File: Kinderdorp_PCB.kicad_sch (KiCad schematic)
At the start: 39 parts, among them J1 Conn_01x08, Q1 2N7002_C306856, U2 AMS1117-3.3_C347222, U5 ESP32-C3-WROOM-02-N4(4MB)

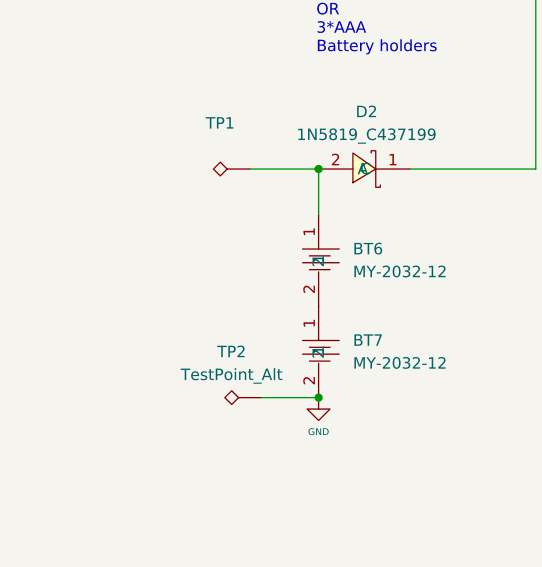
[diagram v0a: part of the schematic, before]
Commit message: added AAA box 3d model and reference images
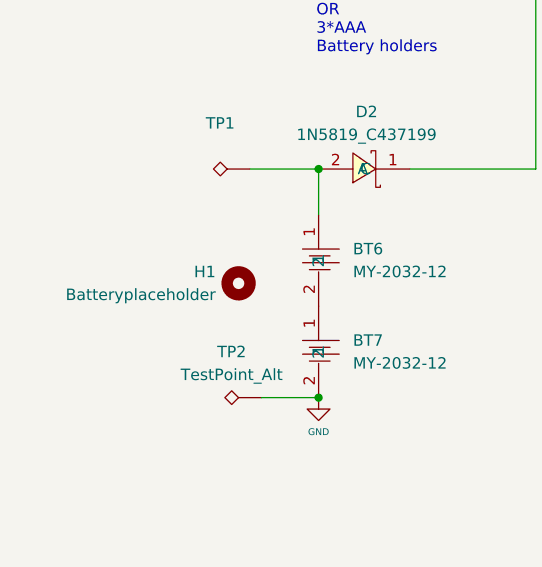
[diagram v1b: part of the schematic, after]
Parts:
- added H1: Batteryplaceholder, Capacitor_Tantalum_SMD:CP_EIA-1608-10_AVX-L, symbol Mechanical:MountingHole
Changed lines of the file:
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@@
+	)
+	(symbol
+		(lib_id "Mechanical:MountingHole")
+		(at 41.91 87.63 0)
+		(unit 1)
+		(exclude_from_sim no)
+		(in_bom no)
+		(on_board yes)
+		(dnp no)
+		(property "Reference" "H1"
+			(at 39.37 86.3599 0)
+			(effects
+				(font
+					(size 1.27 1.27)
+				)
+				(justify right)
+			)
+		)
+		(property "Value" "Batteryplaceholder"
+			(at 39.37 88.8999 0)
+			(effects
+				(font
+					(size 1.27 1.27)
+				)
+				(justify right)
+			)
+		)
+		(property "Footprint" "Capacitor_Tantalum_SMD:CP_EIA-1608-10_AVX-L"
+			(at 41.91 87.63 0)
+			(effects
+				(font
+					(size 1.27 1.27)
+				)
+				(hide yes)
+			)
+		)
+		(property "Datasheet" "~"
+			(at 41.91 87.63 0)
+			(effects
+				(font
+					(size 1.27 1.27)
+				)
+				(hide yes)
+			)
+		)
+		(property "Description" "Mounting Hole without connection"
+			(at 41.91 87.63 0)
+			(effects
+				(font
+					(size 1.27 1.27)
+				)
+				(hide yes)
+			)
+		)
+		(instances
+			(project ""
+				(path "/17f7643f-a16b-4802-8051-c0810a7f40c9"
+					(reference "H1")
+					(unit 1)
+				)
+			)
+		)
 	)
 	(symbol

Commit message: imported/created thumb design
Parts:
- H1: footprint Capacitor_Tantalum_SMD:CP_EIA-1608-10_AVX-L -> MountingHole:MountingHole_2.1mm
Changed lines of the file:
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@@
 			)
 		)
-		(property "Footprint" "Capacitor_Tantalum_SMD:CP_EIA-1608-10_AVX-L"
+		(property "Footprint" "MountingHole:MountingHole_2.1mm"
 			(at 41.91 87.63 0)
 			(effects

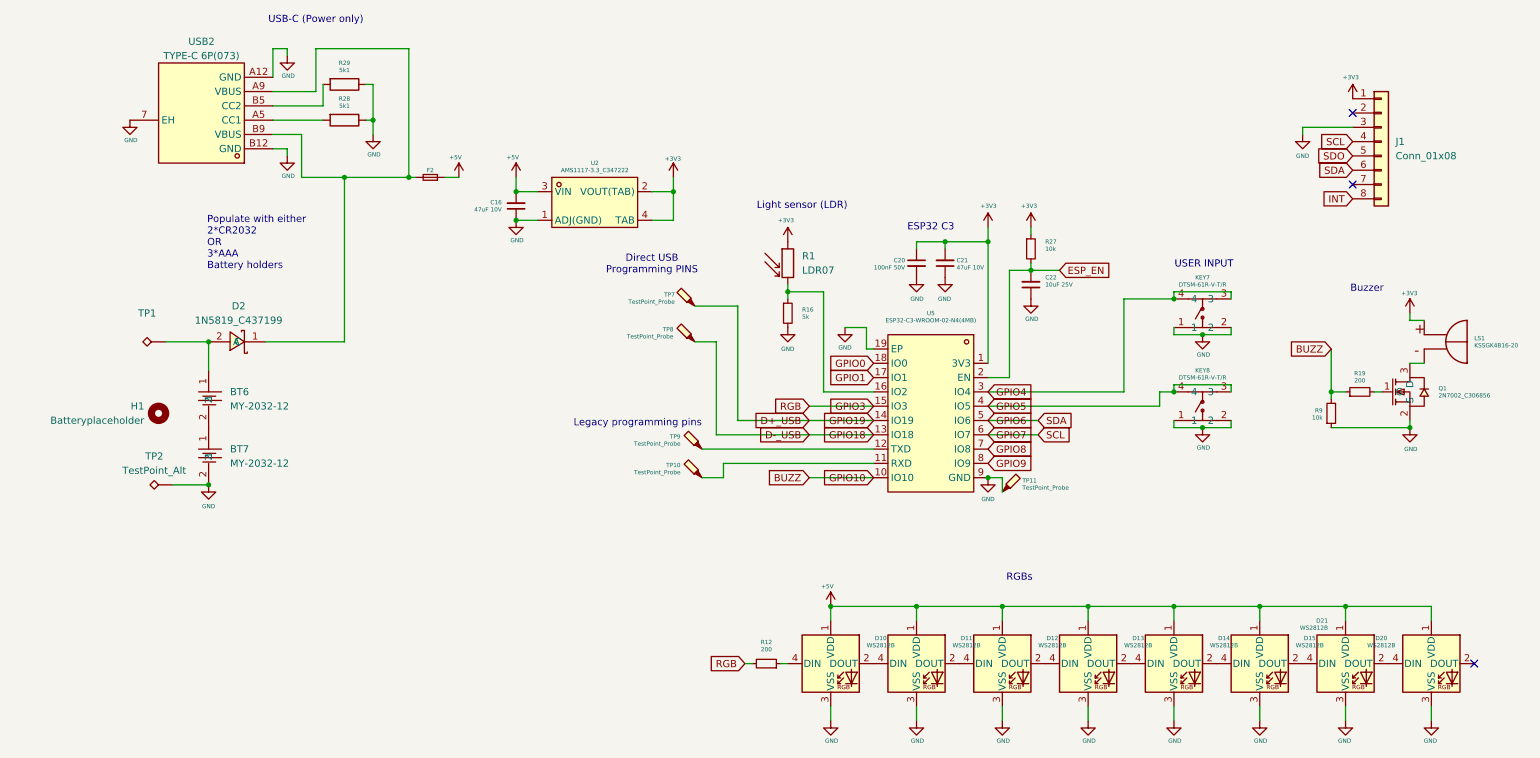
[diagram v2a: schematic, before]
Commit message: fixed naming designators
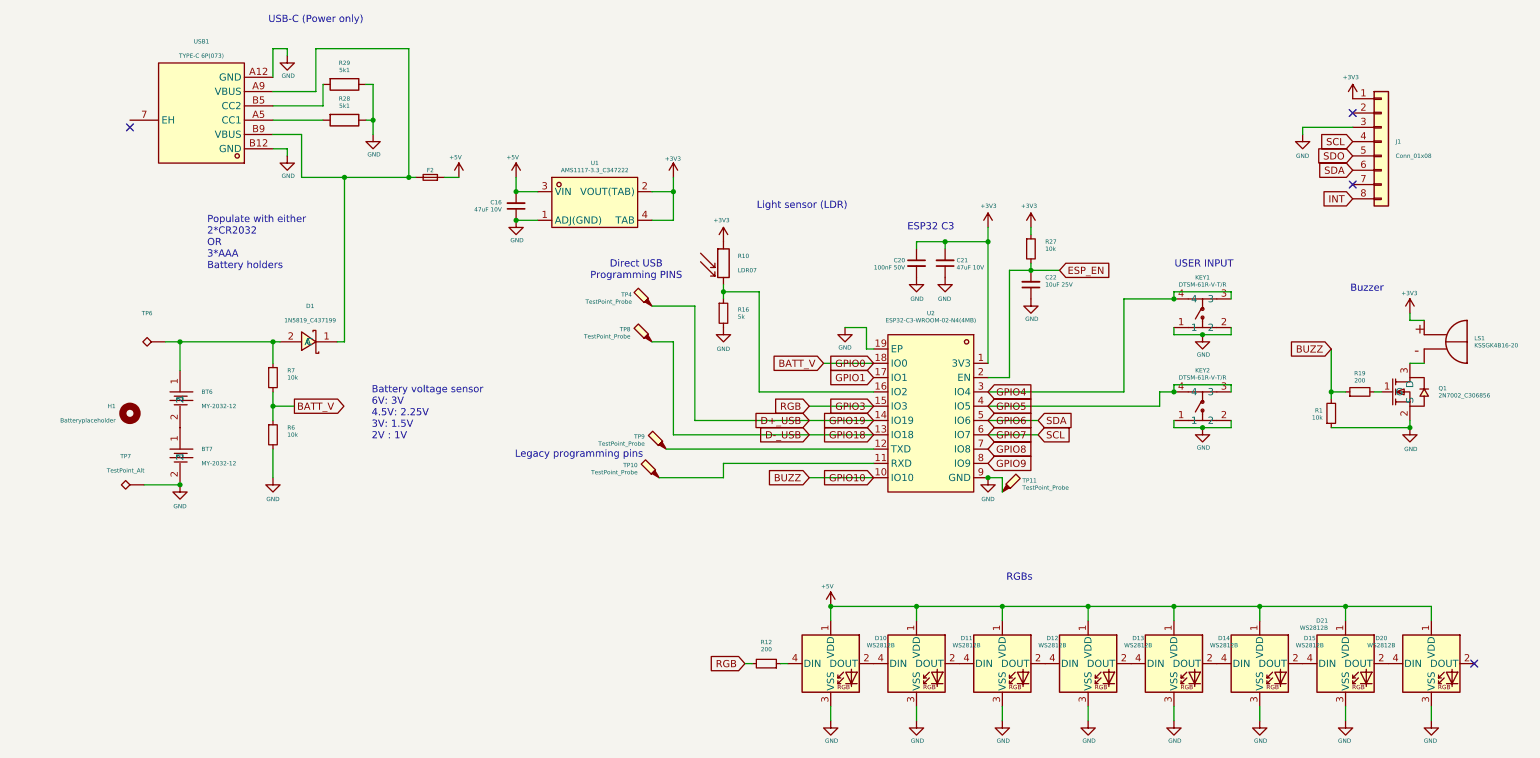
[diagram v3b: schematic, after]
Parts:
- added R6, R7: 10k, Resistor_SMD:R_1206_3216Metric_Pad1.30x1.75mm_HandSolder, symbol Device:R_Small
- renumbered D2 to D1, KEY7 to KEY1, KEY8 to KEY2, R9 to R1, R1 to R10, TP7 to TP4, TP1 to TP6, TP2 to TP7, U2 to U1, U5 to U2, USB2 to USB1
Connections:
- net GND: now also R6.2; no longer USB1.7 (EH)
- net at BT6.1, D1.2 (A), TP6.1: now also R7.1
- net GPIO0 renamed BATT_V
- net BATT_V: now also R6.1, R7.2
- no-connect marks 3 -> 4
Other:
- note added: "Battery voltage sensor 6V: 3V 4.5V: 2.25V 3V: 1.5V 2V : 1V"
- moved on the sheet: BT6, BT7, D1, H1, R10, R16, TP10, TP4, TP7, TP8, TP9

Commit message: fixed annotation again
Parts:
- renumbered BT6 to BT1, BT7 to BT2, KEY1 to BUTTON1, KEY2 to BUTTON2, C16 to C1, C20 to C2, C21 to C3, C22 to C4, F2 to F1, J1 to HDR1, R10 to LDR1, D10 to LED1, D11 to LED2, D12 to LED3, D13 to LED4, D14 to LED5, D15 to LED6, D21 to LED7, D20 to LED8, R7 to R1, R6 to R2, R29 to R3, R28 to R4, R16 to R5, R12 to R6, R27 to R7, R1 to R8, R19 to R9, TP7 to TP1, TP6 to TP2, TP4 to TP3, TP8 to TP4, TP10 to TP5, TP9 to TP6, TP11 to TP7
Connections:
- net Net-(U5-RXD): now reaches TP5.1, U2.11 (RXD)
- net Net-(D2-A): now reaches BT1.1, D1.2 (A), R1.1, TP2.1
- net Net-(U5-TXD): now reaches TP6.1, U2.12 (TXD)

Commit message: finished layout
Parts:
- renumbered TP2 to BATT+1, TP1 to BATT-1, H1 to BATTPACK1, TP3 to USB+, TP4 to USB-
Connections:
- net Net-(D2-A): no longer names the net of BATT+1.1, BT1.1, D1.2 (A), R1.1
- net Net-(U5-RXD): no longer names the net of TP5.1, U2.11 (RXD)
- net Net-(U5-TXD): no longer names the net of TP6.1, U2.12 (TXD)
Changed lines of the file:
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@@
 	(title_block
 		(title "Kinderdorp Printplaat")
-		(date "2025-05-12")
+		(date "2025-07-26")
 		(rev "V1.0")
 		(comment 1 "Casper R. Tak")
@@
 		)
 	)
-	(label "Net-(D2-A)"
-		(at 63.5 74.93 180)
-		(effects
-			(font
-				(size 1.27 1.27)
-			)
-			(justify right bottom)
-		)
-	)
-	(label "Net-(U5-TXD)"
-		(at 168.91 93.98 180)
-		(effects
-			(font
-				(size 1.27 1.27)
-			)
-			(justify right bottom)
-		)
-	)
-	(label "Net-(D2-A)"
-		(at 63.5 74.93 180)
-		(effects
-			(font
-				(size 1.27 1.27)
-			)
-			(justify right bottom)
-		)
-	)
-	(label "Net-(U5-RXD)"
-		(at 168.91 96.52 180)
-		(effects
-			(font
-				(size 1.27 1.27)
-			)
-			(justify right bottom)
-		)
-	)
-	(label "Net-(D2-A)"
-		(at 63.5 74.93 180)
-		(effects
-			(font
-				(size 1.27 1.27)
-			)
-			(justify right bottom)
-		)
-	)
 	(global_label "GPIO6"
 		(shape input)
@@
 		(dnp no)
 		(fields_autoplaced yes)
-		(property "Reference" "TP1"
+		(property "Reference" "BATT-1"
 			(at 36.068 96.52 90)
 			(effects
@@
 			(project "Kinderdorp_PCB"
 				(path "/17f7643f-a16b-4802-8051-c0810a7f40c9"
-					(reference "TP1")
+					(reference "BATT-1")
 					(unit 1)
 				)
@@
 		(dnp no)
 		(fields_autoplaced yes)
-		(property "Reference" "TP4"
+		(property "Reference" "USB-"
 			(at 125.73 72.7074 0)
 			(effects
@@
 			(project "Kinderdorp_PCB"
 				(path "/17f7643f-a16b-4802-8051-c0810a7f40c9"
-					(reference "TP4")
+					(reference "USB-")
 					(unit 1)
 				)
@@
 		(dnp no)
 		(fields_autoplaced yes)
-		(property "Reference" "TP3"
+		(property "Reference" "USB+"
 			(at 130.81 66.3574 0)
 			(effects
@@
 			(project "Kinderdorp_PCB"
 				(path "/17f7643f-a16b-4802-8051-c0810a7f40c9"
-					(reference "TP3")
+					(reference "USB+")
 					(unit 1)
 				)
@@
 		(dnp no)
 		(fields_autoplaced yes)
-		(property "Reference" "H1"
+		(property "Reference" "BATTPACK1"
 			(at 36.83 82.55 0)
 			(effects
@@
 			(project ""
 				(path "/17f7643f-a16b-4802-8051-c0810a7f40c9"
-					(reference "H1")
+					(reference "BATTPACK1")
 					(unit 1)
 				)
@@
 		(dnp no)
 		(fields_autoplaced yes)
-		(property "Reference" "TP2"
+		(property "Reference" "BATT+1"
 			(at 39.878 71.12 90)
 			(effects
@@
 			(project ""
 				(path "/17f7643f-a16b-4802-8051-c0810a7f40c9"
-					(reference "TP2")
+					(reference "BATT+1")
 					(unit 1)
 				)

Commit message: updated logo
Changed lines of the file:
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@@
 	)
 	(no_connect
-		(at 36.83 36.83)
+		(at 36.83 35.56)
 	)
 	(no_connect
@@
 		(on_board yes)
 		(dnp no)
-		(fields_autoplaced yes)
 		(property "Reference" "TP6"
 			(at 128.27 91.7574 0)
@@
 					(size 0.75 0.75)
 				)
-				(justify left)
+				(justify right)
 			)
 		)

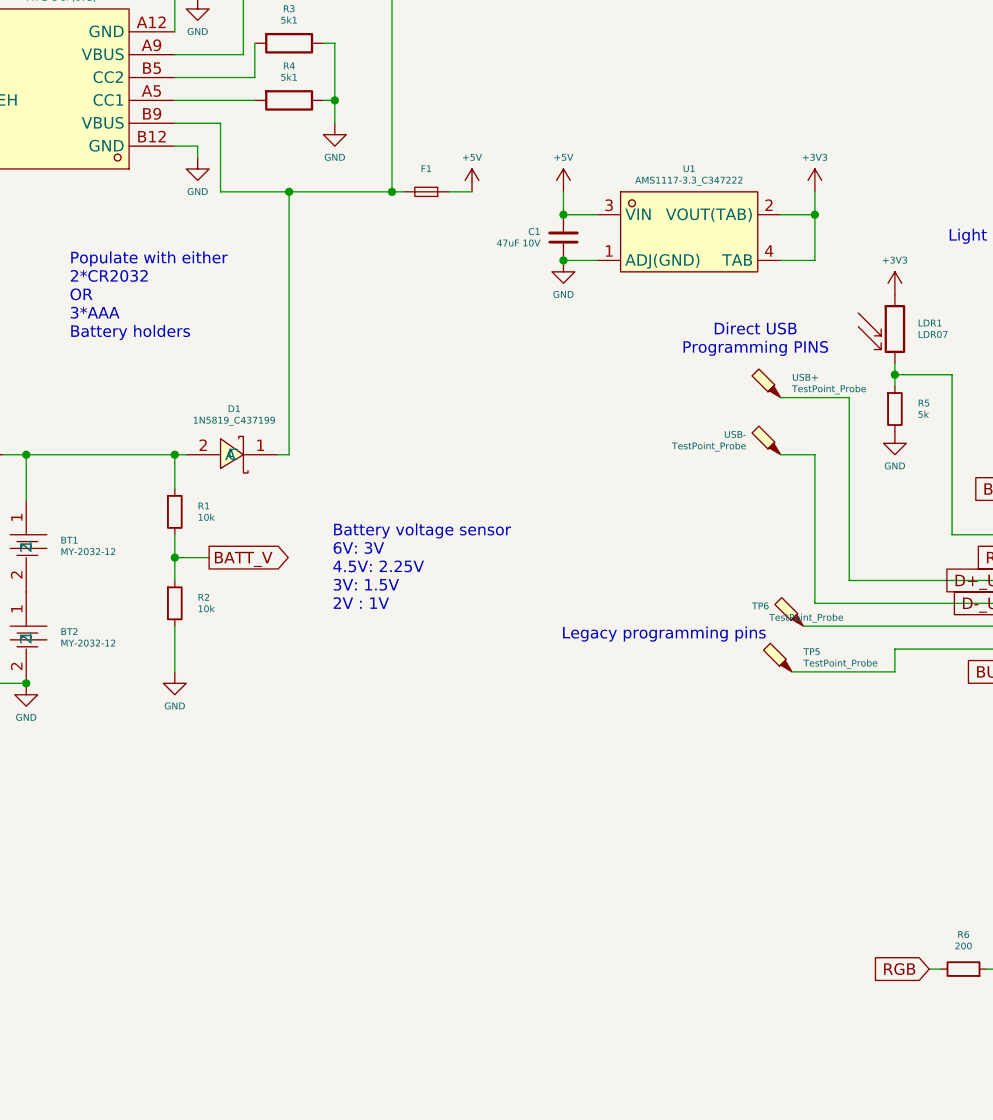
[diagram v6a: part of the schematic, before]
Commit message: Finalized design
- added esd protection
- minor silkscreen improvements
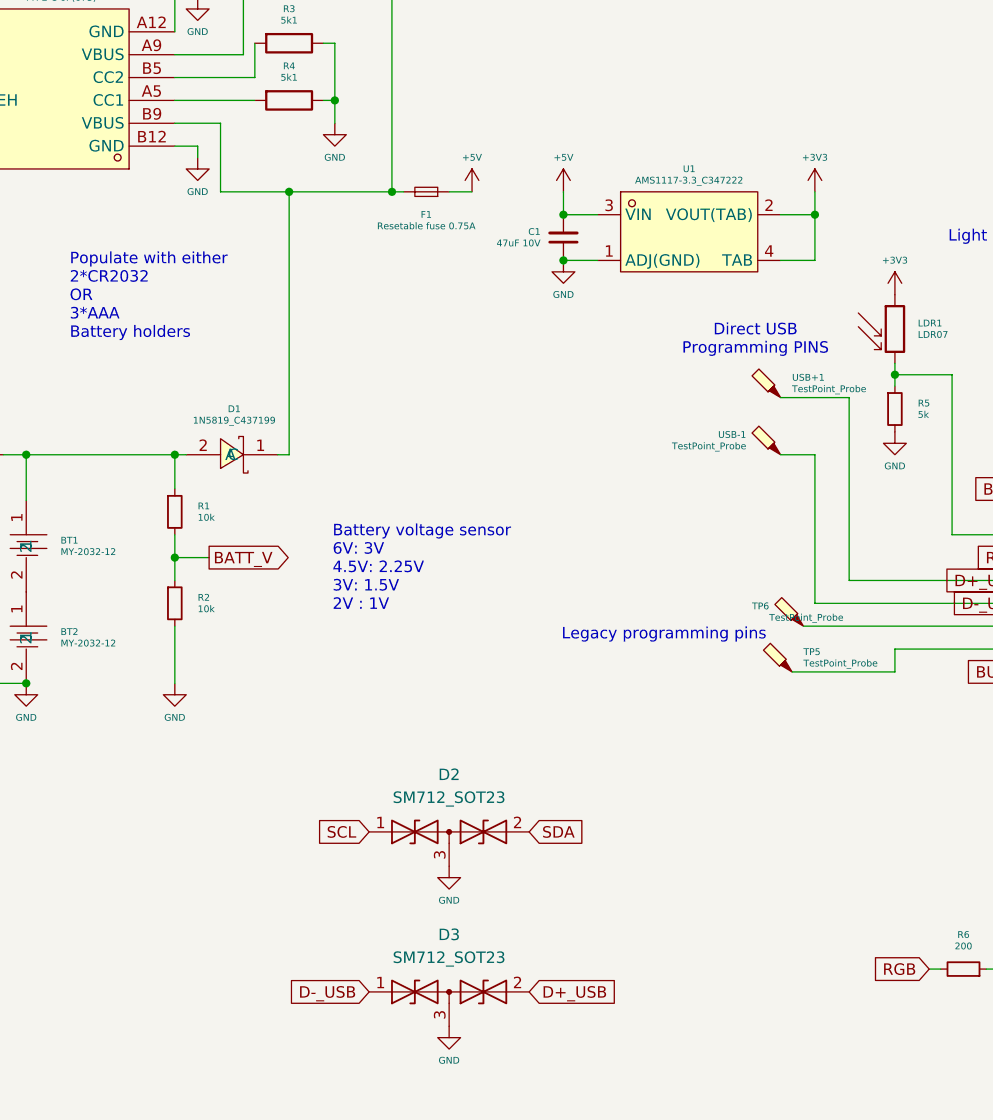
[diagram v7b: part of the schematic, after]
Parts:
- added D2, D3: SM712_SOT23, Package_TO_SOT_SMD:SOT-23, symbol Diode:SM712_SOT23
- F1: value Fuse_Small 2A -> Resetable fuse 0.75A
- renumbered USB+ to USB+1, USB- to USB-1
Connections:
- net D+_USB: now also D3.2 (A2)
- net D-_USB: now also D3.1 (A1)
- net GND: now also D2.3 (common), D3.3 (common)
- net GPIO6: now also D2.2 (A2)
- net GPIO7: now also D2.1 (A1)

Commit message: minor changes to files and added production files
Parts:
- R9: value 200 -> 100
- renumbered BATT+1 to BATT+, BATT-1 to BATT-, USB+1 to USB+, USB-1 to USB-
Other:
- note added: "5V -> 3.3V DC/DC converter"
- note added: "Buttons"
- note added: "ESD protection"
- note added: "GPIO header"
- note added: "Microcontroller"
- note added: "Populate with either 2*CR2032 OR 3/4*AAA Battery holders"
- note added: "RGB LEDs"
- note removed: "ESP32 C3"
- note removed: "Populate with either 2*CR2032 OR 3*AAA Battery holders"
- note removed: "RGBs"
- note removed: "USER INPUT"
- title: Kinderdorp Printplaat -> Kinderdorp_PCB
- moved on the sheet: C1, U1
